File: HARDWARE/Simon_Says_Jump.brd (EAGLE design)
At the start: 64.8 x 99.1 mm, 62 parts, among them J1 RJ45, J10 B3, J11 LED_CTRLS, J12 5V, J13 5V, J14 B4, J15 B5, J16 B6, J17 B7, J19 12V, J2 RJ45, J20 RJ45, J21 12V, J22 12V, J3 RJ45, J4 RJ45, J6 5V, J8 B1, J9 B2, Q1 NPN, Q2 P-Channel MOSFET, Q3 NPN, Q4 P-Channel MOSFET, Q5 NPN, Q6 P-Channel MOSFET, Q7 NPN, Q8 P-Channel MOSFET, U1 5V Pro Mini, U2 LOGIC

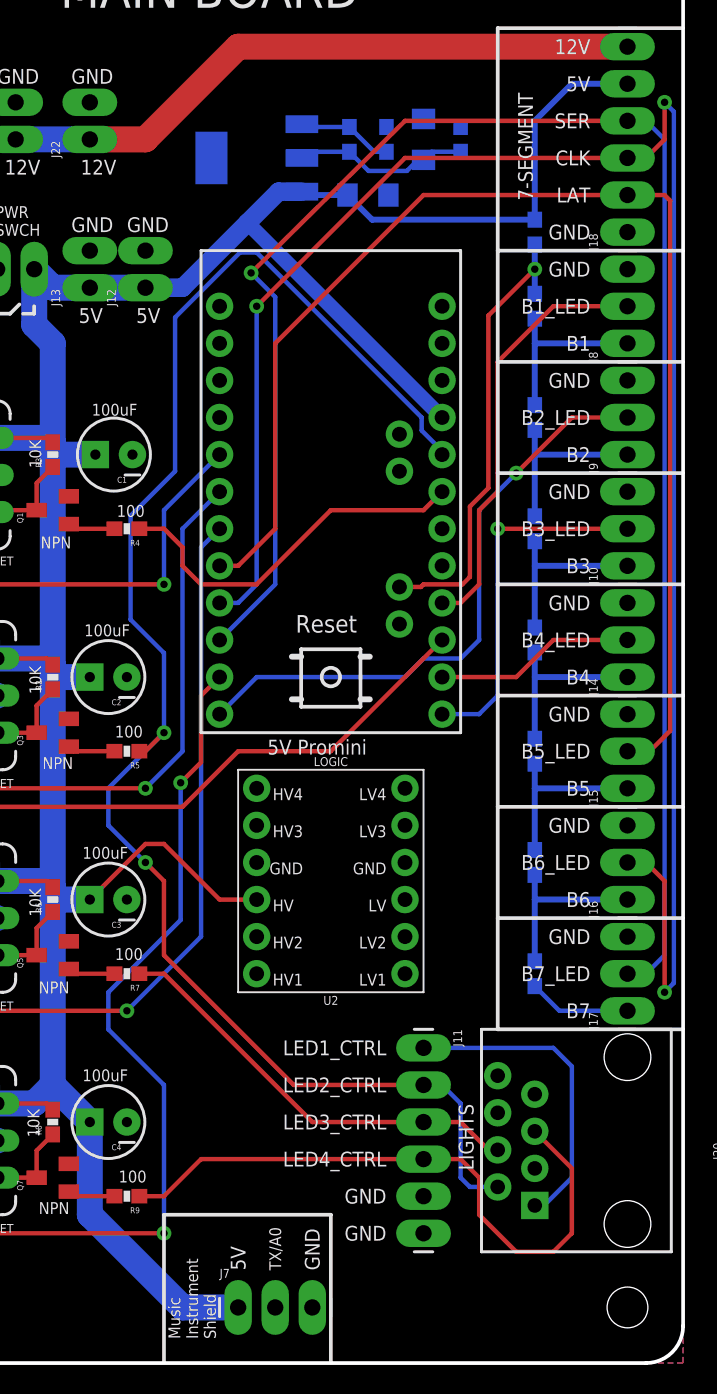
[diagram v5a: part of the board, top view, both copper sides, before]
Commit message: Layout on main board complete
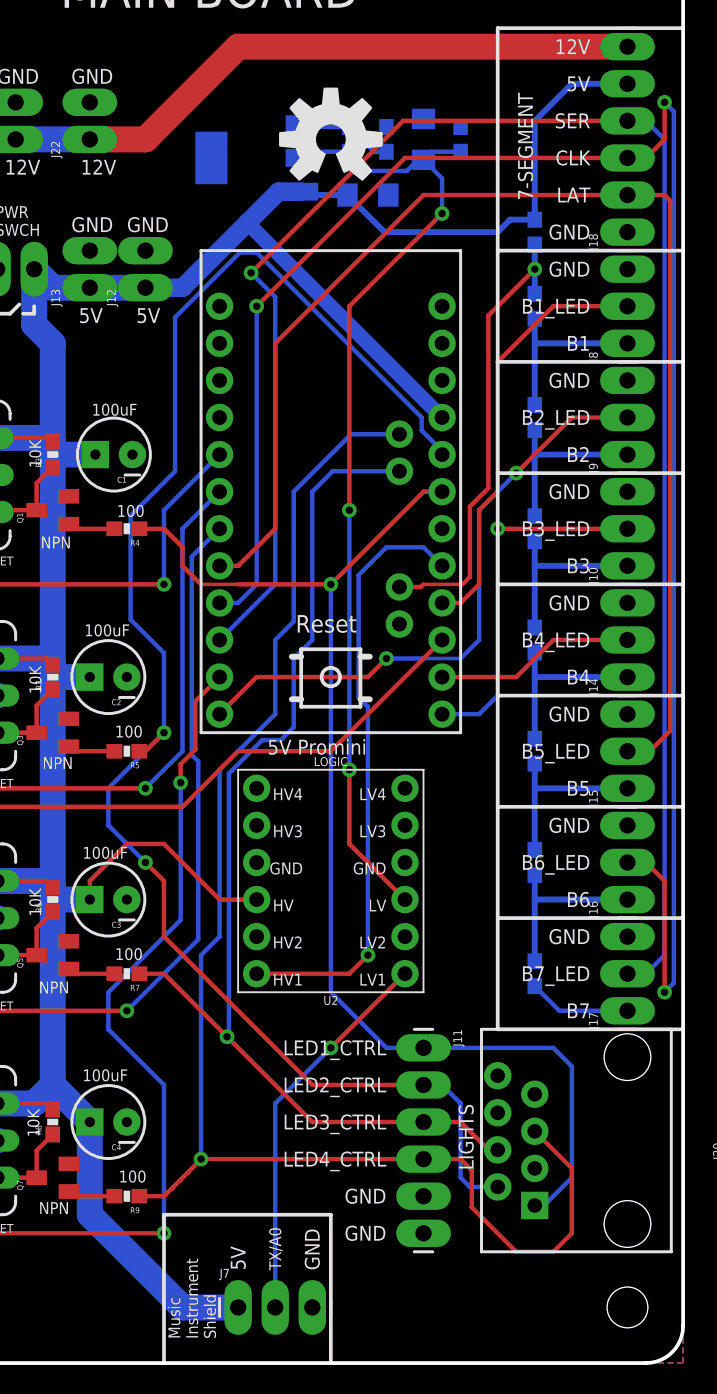
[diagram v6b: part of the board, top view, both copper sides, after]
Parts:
- added LOGO1: OSHW-LOGOL, SparkFun-Aesthetics:OSHW-LOGO-L
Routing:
- net LED4_CTRL: track 43.4 -> 100.6 mm, vias 0 -> 1
- net 3.3V: track 12.1 -> 67.5 mm, vias 0 -> 3
- net LED3_CTRL: track 29.5 -> 76.6 mm, vias 0 -> 1
- net SW_SER_TX: track 0.00 -> 41.5 mm, vias 0 -> 1
- net LED1_CTRL: track 47.3 -> 83.2 mm, vias 0 -> 1
- net SW_SER_TX_3.3V: track 0.00 -> 26.5 mm, vias 0 -> 1
- net 5V: track 244.7 -> 246.1 mm
- net LED2_CTRL: track 110.2 -> 109.5 mm
- net B2_LED: vias 1 -> 2
